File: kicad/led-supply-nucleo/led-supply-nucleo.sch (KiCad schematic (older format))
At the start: 0 parts

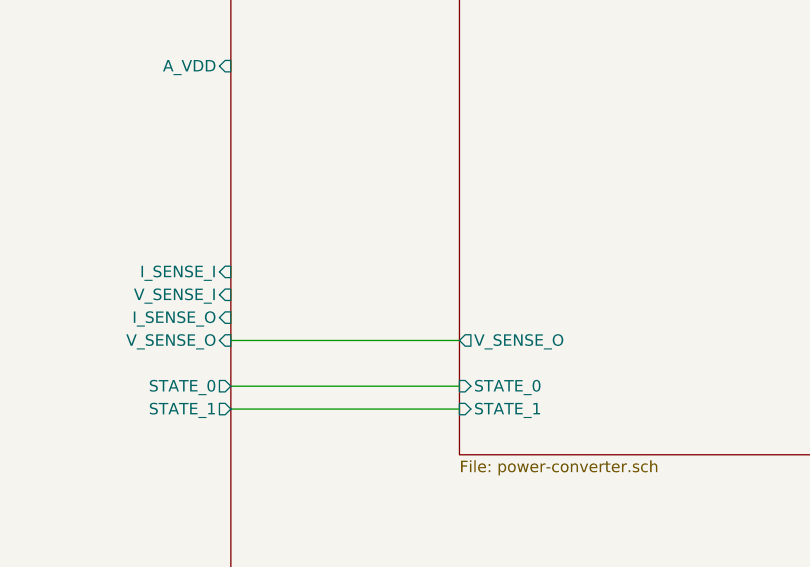
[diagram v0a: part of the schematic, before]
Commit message: Add Nucleo based board for prototyping.
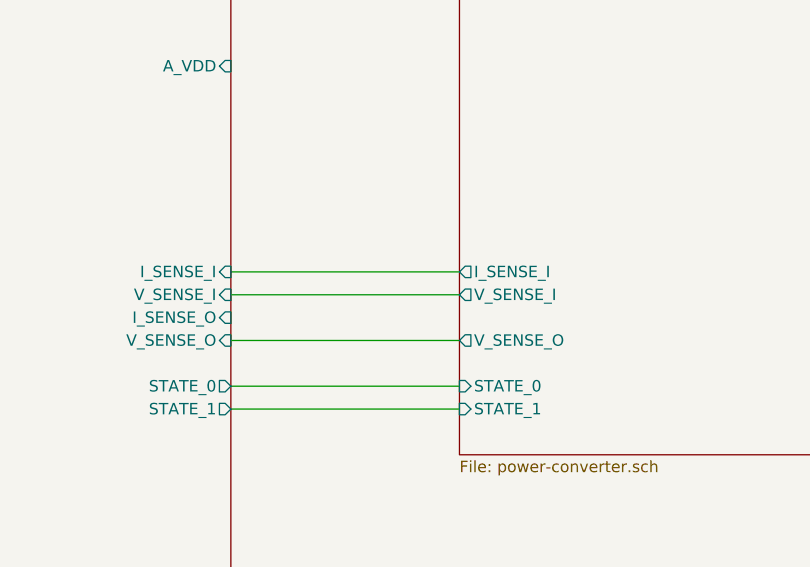
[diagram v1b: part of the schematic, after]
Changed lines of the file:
@@
 F9 "DRV_Q5" I L 4500 2400 50
 F10 "DRV_Q6" I L 4500 2500 50
+F11 "I_SENSE_I" O L 4500 5200 50
+F12 "V_SENSE_I" O L 4500 5300 50
 $EndSheet
 $Sheet
@@
 Wire Wire Line
 	3500 2500 4500 2500
+Wire Wire Line
+	3500 5300 4500 5300
+Wire Wire Line
+	3500 5200 4500 5200
 $EndSCHEMATC
